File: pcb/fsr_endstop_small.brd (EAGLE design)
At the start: 27.9 x 30.5 mm, 33 parts, among them U1 ATTINY461

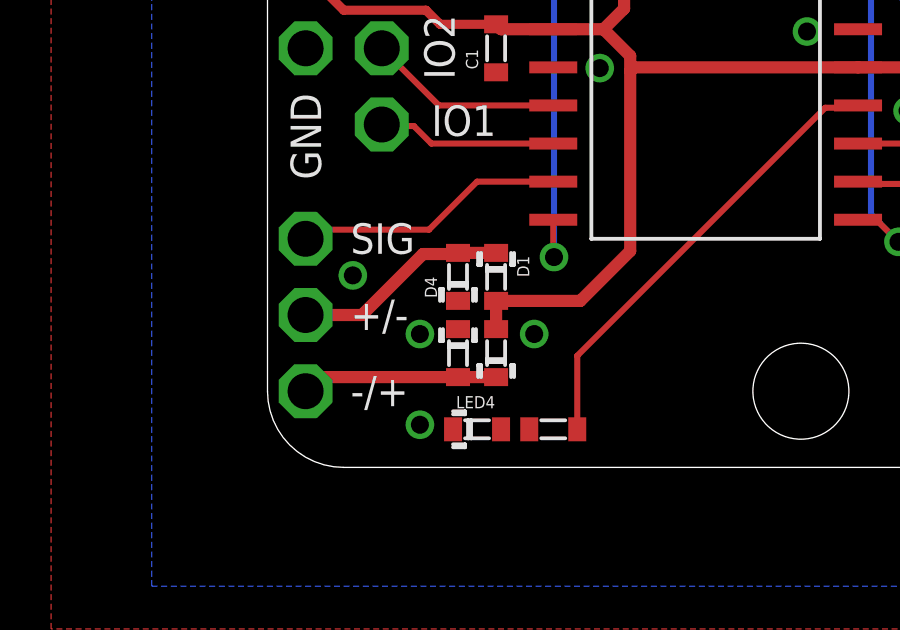
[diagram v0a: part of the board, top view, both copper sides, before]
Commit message: Reverse polarity of diodes
Diodes were backwards in the schematic for the bridge rectifier.
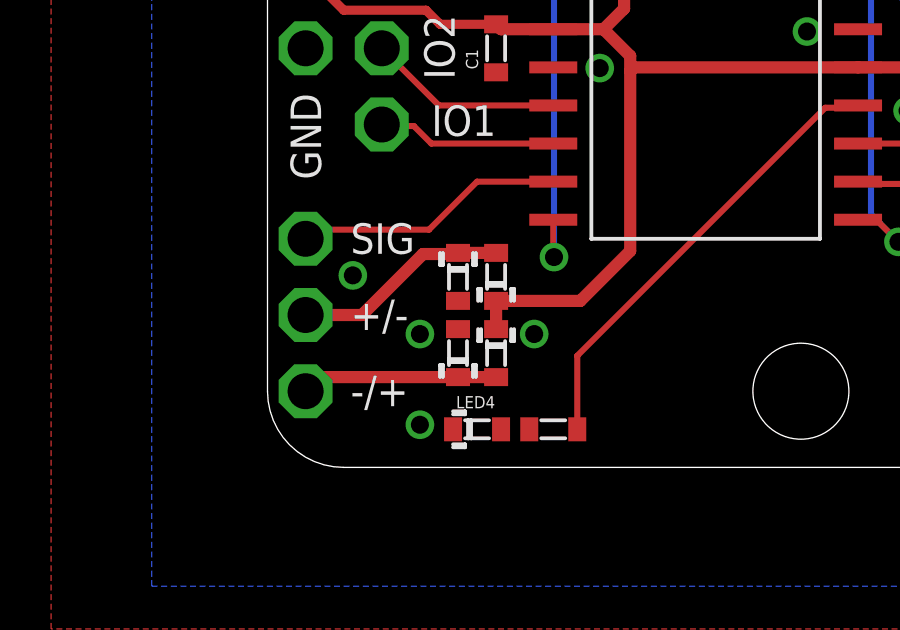
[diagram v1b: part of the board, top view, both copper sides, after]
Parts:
- turned D1 to 90 degrees
- turned D2 to 270 degrees
- turned D3 to 90 degrees
- turned D4 to 270 degrees
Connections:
- net GND: now also D3.+, D4.+; no longer D3.-, D4.-
- net N$3: now also D2.+, D3.-; no longer D2.-, D3.+
- net N$4: now also D1.+, D4.-; no longer D1.-, D4.+
- net V+: now also D1.-, D2.-; no longer D1.+, D2.+
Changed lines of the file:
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@@
 <setting verticaltext="up"/>
 </settings>
-<grid distance="0.025" unitdist="inch" unit="inch" style="dots" multiple="4" display="yes" altdistance="0.025" altunitdist="inch" altunit="inch"/>
+<grid distance="0.025" unitdist="inch" unit="inch" style="dots" multiple="1" display="yes" altdistance="0.025" altunitdist="inch" altunit="inch"/>
 <layers>
 <layer number="1" name="Top" color="4" fill="1" visible="yes" active="yes"/>
@@
 <attribute name="NAME" x="15.4432" y="32.1818" size="1.27" layer="25" font="vector"/>
 </element>
-<element name="D1" library="_sg_lib" package="0603_DIODE" value="" x="20.32" y="19.05" rot="R270"/>
-<element name="D2" library="_sg_lib" package="0603_DIODE" value="" x="20.32" y="16.51" smashed="yes" rot="R90">
-<attribute name="NAME" x="21.5504" y="15.81" size="0.4064" layer="25" font="vector" rot="R90"/>
-<attribute name="NAME" x="21.4392" y="15.9132" size="0.3048" layer="51" font="vector" rot="R90"/>
-<attribute name="VALUE" x="20.62" y="15.71" size="0.3048" layer="51" font="vector" rot="R90"/>
-</element>
-<element name="D3" library="_sg_lib" package="0603_DIODE" value="" x="19.05" y="16.51" smashed="yes" rot="R270">
-<attribute name="NAME" x="17.9212" y="16.6004" size="0.4064" layer="25" font="vector" rot="R270"/>
-<attribute name="NAME" x="18.0324" y="16.3956" size="0.3048" layer="51" font="vector" rot="R270"/>
-<attribute name="VALUE" x="18.75" y="17.31" size="0.3048" layer="51" font="vector" rot="R270"/>
-</element>
-<element name="D4" library="_sg_lib" package="0603_DIODE" value="" x="19.05" y="19.05" rot="R90"/>
+<element name="D1" library="_sg_lib" package="0603_DIODE" value="" x="20.32" y="19.05" smashed="yes" rot="R90">
+<attribute name="NAME" x="21.02" y="19.75" size="0.4064" layer="25" font="vector" rot="R270"/>
+<attribute name="NAME" x="20.22" y="18.25" size="0.3048" layer="51" font="vector" rot="R90"/>
+<attribute name="VALUE" x="20.62" y="18.25" size="0.3048" layer="51" font="vector" rot="R90"/>
+</element>
+<element name="D2" library="_sg_lib" package="0603_DIODE" value="" x="20.32" y="16.51" smashed="yes" rot="R270">
+<attribute name="NAME" x="20.9946" y="16.575" size="0.4064" layer="25" font="vector" rot="R270"/>
+<attribute name="NAME" x="19.2008" y="17.1068" size="0.3048" layer="51" font="vector" rot="R270"/>
+<attribute name="VALUE" x="20.02" y="17.31" size="0.3048" layer="51" font="vector" rot="R270"/>
+</element>
+<element name="D3" library="_sg_lib" package="0603_DIODE" value="" x="19.05" y="16.51" smashed="yes" rot="R90">
+<attribute name="NAME" x="18.2738" y="15.7846" size="0.4064" layer="25" font="vector" rot="R90"/>
+<attribute name="NAME" x="20.0676" y="16.6244" size="0.3048" layer="51" font="vector" rot="R90"/>
+<attribute name="VALUE" x="19.35" y="15.71" size="0.3048" layer="51" font="vector" rot="R90"/>
+</element>
+<element name="D4" library="_sg_lib" package="0603_DIODE" value="" x="19.05" y="19.05" smashed="yes" rot="R270">
+<attribute name="NAME" x="18.35" y="18.35" size="0.4064" layer="25" font="vector" rot="R90"/>
+<attribute name="NAME" x="19.15" y="19.85" size="0.3048" layer="51" font="vector" rot="R270"/>
+<attribute name="VALUE" x="18.75" y="19.85" size="0.3048" layer="51" font="vector" rot="R270"/>
+</element>
 <element name="C1" library="_sg_lib" package="0603" value="1uF" x="20.32" y="26.67" rot="R90"/>
 <element name="LED1" library="_sg_lib" package="0603_DIODE" value="LED0603" x="36.195" y="36.195" rot="R90"/>
@@
 <signals>
 <signal name="N$3">
-<contactref element="D3" pad="+"/>
-<contactref element="D2" pad="-"/>
 <contactref element="-/+" pad="P$1"/>
-<wire x1="20.32" y1="15.71" x2="19.05" y2="15.71" width="0.4064" layer="1"/>
-<wire x1="19.05" y1="15.71" x2="14.44" y2="15.71" width="0.4064" layer="1"/>
 <wire x1="14.44" y1="15.71" x2="13.97" y2="15.24" width="0.4064" layer="1"/>
+<contactref element="D2" pad="+"/>
+<contactref element="D3" pad="-"/>
+<wire x1="14.44" y1="15.71" x2="19.05" y2="15.71" width="0.4064" layer="1"/>
+<wire x1="19.05" y1="15.71" x2="20.32" y2="15.71" width="0.4064" layer="1"/>
 </signal>
 <signal name="N$4">
 <contactref element="+/-" pad="P$1"/>
-<contactref element="D1" pad="-"/>
-<contactref element="D4" pad="+"/>
-<wire x1="20.32" y1="19.85" x2="19.05" y2="19.85" width="0.4064" layer="1"/>
 <wire x1="13.97" y1="17.78" x2="15.8496" y2="17.78" width="0.4064" layer="1"/>
 <wire x1="15.8496" y1="17.78" x2="17.8816" y2="19.812" width="0.4064" layer="1"/>
-<wire x1="17.8816" y1="19.812" x2="19.012" y2="19.812" width="0.4064" layer="1"/>
-<wire x1="19.012" y1="19.812" x2="19.05" y2="19.85" width="0.4064" layer="1"/>
+<contactref element="D1" pad="+"/>
+<contactref element="D4" pad="-"/>
+<wire x1="17.8816" y1="19.812" x2="19.05" y2="19.812" width="0.4064" layer="1"/>
+<wire x1="19.05" y1="19.812" x2="19.05" y2="19.85" width="0.4064" layer="1"/>
+<wire x1="19.05" y1="19.85" x2="20.32" y2="19.85" width="0.4064" layer="1"/>
 </signal>
 <signal name="V+">
-<contactref element="D2" pad="+"/>
-<contactref element="D1" pad="+"/>
 <contactref element="U1" pad="P$15"/>
 <contactref element="C1" pad="2"/>
@@
 <contactref element="VCC" pad="P$1"/>
 <contactref element="C2" pad="2"/>
-<wire x1="20.32" y1="17.31" x2="20.32" y2="18.25" width="0.4064" layer="1"/>
-<wire x1="20.32" y1="18.25" x2="23.1268" y2="18.25" width="0.4064" layer="1"/>
 <wire x1="23.1268" y1="18.25" x2="24.7904" y2="19.9136" width="0.4064" layer="1"/>
 <wire x1="24.7904" y1="19.9136" x2="24.7904" y2="25.908" width="0.4064" layer="1"/>
@@
 <wire x1="39.8272" y1="34.036" x2="39.8272" y2="39.7128" width="0.3048" layer="1"/>
 <wire x1="39.8272" y1="39.7128" x2="38.1" y2="41.44" width="0.3048" layer="1"/>
+<contactref element="D1" pad="-"/>
+<contactref element="D2" pad="-"/>
+<wire x1="23.1268" y1="18.25" x2="20.32" y2="18.25" width="0.4064" layer="1"/>
+<wire x1="20.32" y1="18.25" x2="20.32" y2="17.31" width="0.4064" layer="1"/>
 </signal>
 <signal name="GND">
-<contactref element="D4" pad="-"/>
-<contactref element="D3" pad="-"/>
 <contactref element="C1" pad="1"/>
 <contactref element="U1" pad="P$6"/>
@@
 <via x="34.036" y="24.5872" extent="1-16" drill="0.6"/>
 <via x="15.5448" y="19.1008" extent="1-16" drill="0.6"/>
+<contactref element="D4" pad="+"/>
+<contactref element="D3" pad="+"/>
 </signal>
 <signal name="N$1">
